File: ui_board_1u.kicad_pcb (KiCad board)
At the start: 2 copper layers, 156 x 38 mm, 121 parts, among them J1 X9555WV-2x06-6TV01, J5 BM07B-SRSS-TB, SW1 ZX-QC66-7.5TP, SW2 291V1022F832AB, SW3 PEC164220F-S0024, SW4 MS-22C01-G010, U1 AFC01-S30FCA-00, U2 SPX3819M5-L, U3 TPS61040DBV, U4 MCP23S17_ML

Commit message: Make button cap longer. Update 3D models
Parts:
- SW1: value ZX-QC66-7.5TP -> B3FS-1052
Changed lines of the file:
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@@
 			)
 		)
-		(property "Value" "ZX-QC66-7.5TP"
+		(property "Value" "B3FS-1052"
 			(at 0 4.2 90)
 			(layer "F.Fab")
@@
 			)
 		)
+		(model "${KIPRJMOD}/cad/step/button_cap.step"
+			(offset
+				(xyz 0 0 4.4)
+			)
+			(scale
+				(xyz 1 1 1)
+			)
+			(rotate
+				(xyz -0 -0 -0)
+			)
+		)
 	)
 	(footprint "a_psu:mouse_bite"
@@
 			)
 		)
+		(model "${KIPRJMOD}/cad/step/oled_panel_2.8inch.step"
+			(offset
+				(xyz 23.9 -43.7 73.52)
+			)
+			(scale
+				(xyz 1 1 1)
+			)
+			(rotate
+				(xyz -180 -0 -180)
+			)
+		)
+		(model "${KIPRJMOD}/cad/step/example_front_panel_2u.step"
+			(offset
+				(xyz -347.5 -44 11)
+			)
+			(scale
+				(xyz 1 1 1)
+			)
+			(rotate
+				(xyz -0 -0 -0)
+			)
+		)
 	)
 	(footprint "kibuzzard-693D4C4F"
@@
 				(font
 					(size 0.001 0.001)
+					(thickness 0.15)
 				)
 				(justify mirror)
@@
 				(font
 					(size 0.001 0.001)
+					(thickness 0.15)
 				)
 				(justify mirror)

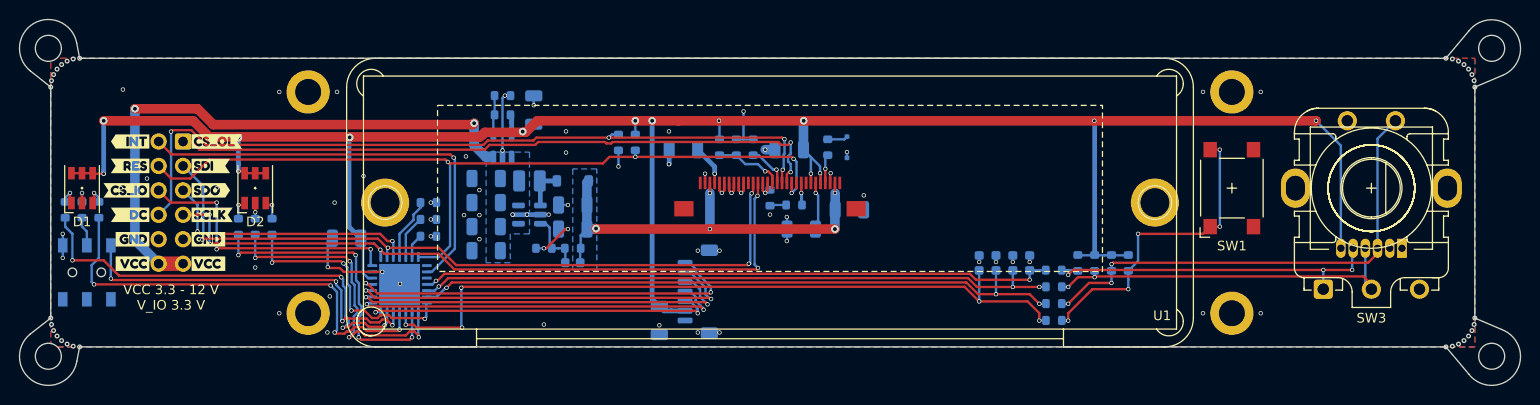
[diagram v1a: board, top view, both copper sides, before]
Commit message: fine tune ext. con position and silk screen
rev - ready to order
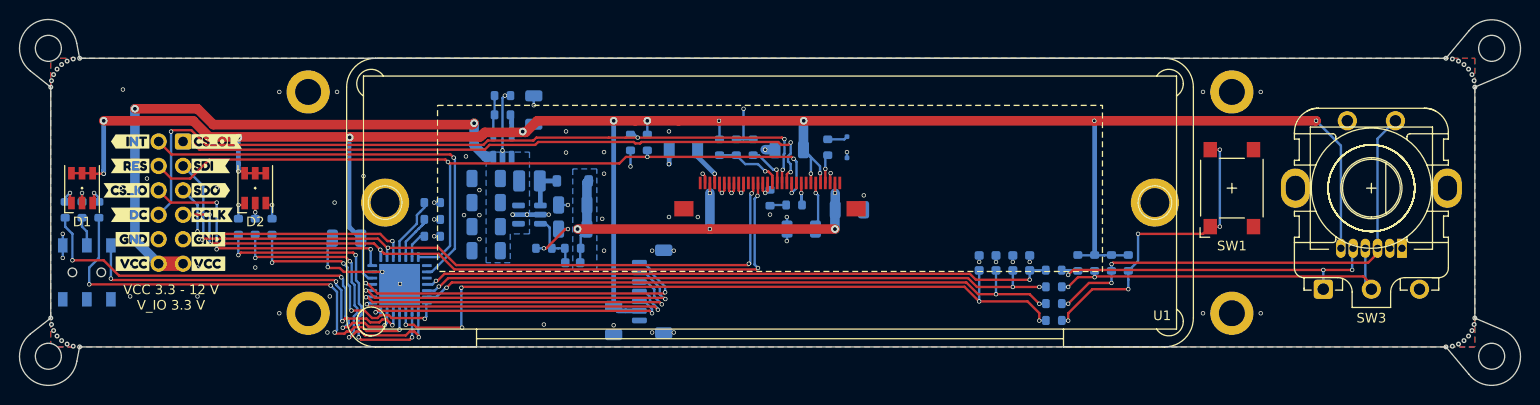
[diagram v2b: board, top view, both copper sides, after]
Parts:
- removed kibuzzard-694336A4: G***, kibuzzard-694336A4
- added kibuzzard-69483936: G***, kibuzzard-69483936, B.Cu at (114.3, 81.3)
- moved C17 4.75 mm to (109.3, 90.8)
- moved J5 4.75 mm to (113.3, 87.8)
- moved R3 1.25 mm to (112.8, 72.3)
- moved R4 1.25 mm to (111.0, 72.3)
- moved R11 0.40 mm to (90.4, 78.5)
- moved R15 0.40 mm to (90.4, 82.0)
- moved R16 0.40 mm to (90.4, 80.3)
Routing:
- net /Switches and LEDs/GPB4: track 38.9 -> 34.1 mm
- net /Switches and LEDs/GPB6: track 41.2 -> 36.4 mm
- net /Switches and LEDs/GPB5: track 40.2 -> 35.5 mm
- net /Switches and LEDs/GPB3: track 36.3 -> 31.6 mm
- net /Switches and LEDs/GPB7: track 41.5 -> 36.8 mm
- net +12V: track 44.1 -> 45.2 mm
- net Net-(U4-A1): track 4.54 -> 5.42 mm
- net GND: track 60.7 -> 60.0 mm, vias 66 -> 76
- net /Switches and LEDs/LEDA_R: track 46.4 -> 46.9 mm

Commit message: add drawing for front-panel cut-outs in User.Comments and Eco1 layers
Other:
- board text added: "Board outline"
- board text added: "Legacy mounting holes"
- board text added: "Mounting holes"
- board text added: "depth = 2.0"
